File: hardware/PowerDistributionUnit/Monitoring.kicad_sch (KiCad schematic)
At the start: 19 parts, among them U32 ADS7953SBDBT, U33 MCP23S17-E/SS, U34 REF4132, U35 TLV9301xDBV

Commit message: added datasheets and footprints to PowerDistributionUnitLib symbol library
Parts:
- U32: footprint (none) -> Package_SO:TSSOP-38_4.4x9.7mm_P0.5mm
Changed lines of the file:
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@@
 			)
 		)
-		(property "Datasheet" ""
+		(property "Datasheet" "${KIPRJMOD}/lib/docs/ref4132.pdf"
 			(at 73.66 35.56 0)
 			(effects
@@
 			)
 		)
-		(property "Footprint" ""
+		(property "Footprint" "Package_SO:TSSOP-38_4.4x9.7mm_P0.5mm"
 			(at 111.76 80.01 0)
 			(effects
@@
 			)
 		)
-		(property "Datasheet" "https://www.ti.com/lit/ds/symlink/ads7953.pdf?ts=1728140483665&ref_url=https%253A%252F%252Fwww.ti.com%252Fproduct%252FADS7953%252Fpart-details%252FADS7953SBDBT"
+		(property "Datasheet" "${KIPRJMOD}/lib/docs/ads7953.pdf"
 			(at 111.76 80.01 0)
 			(effects
@@
 			)
 		)
-		(property "Datasheet" ""
+		(property "Datasheet" "${KIPRJMOD}/lib/docs/MCP23017-Data-Sheet-DS20001952-1.pdf"
 			(at 211.582 61.214 0)
 			(effects

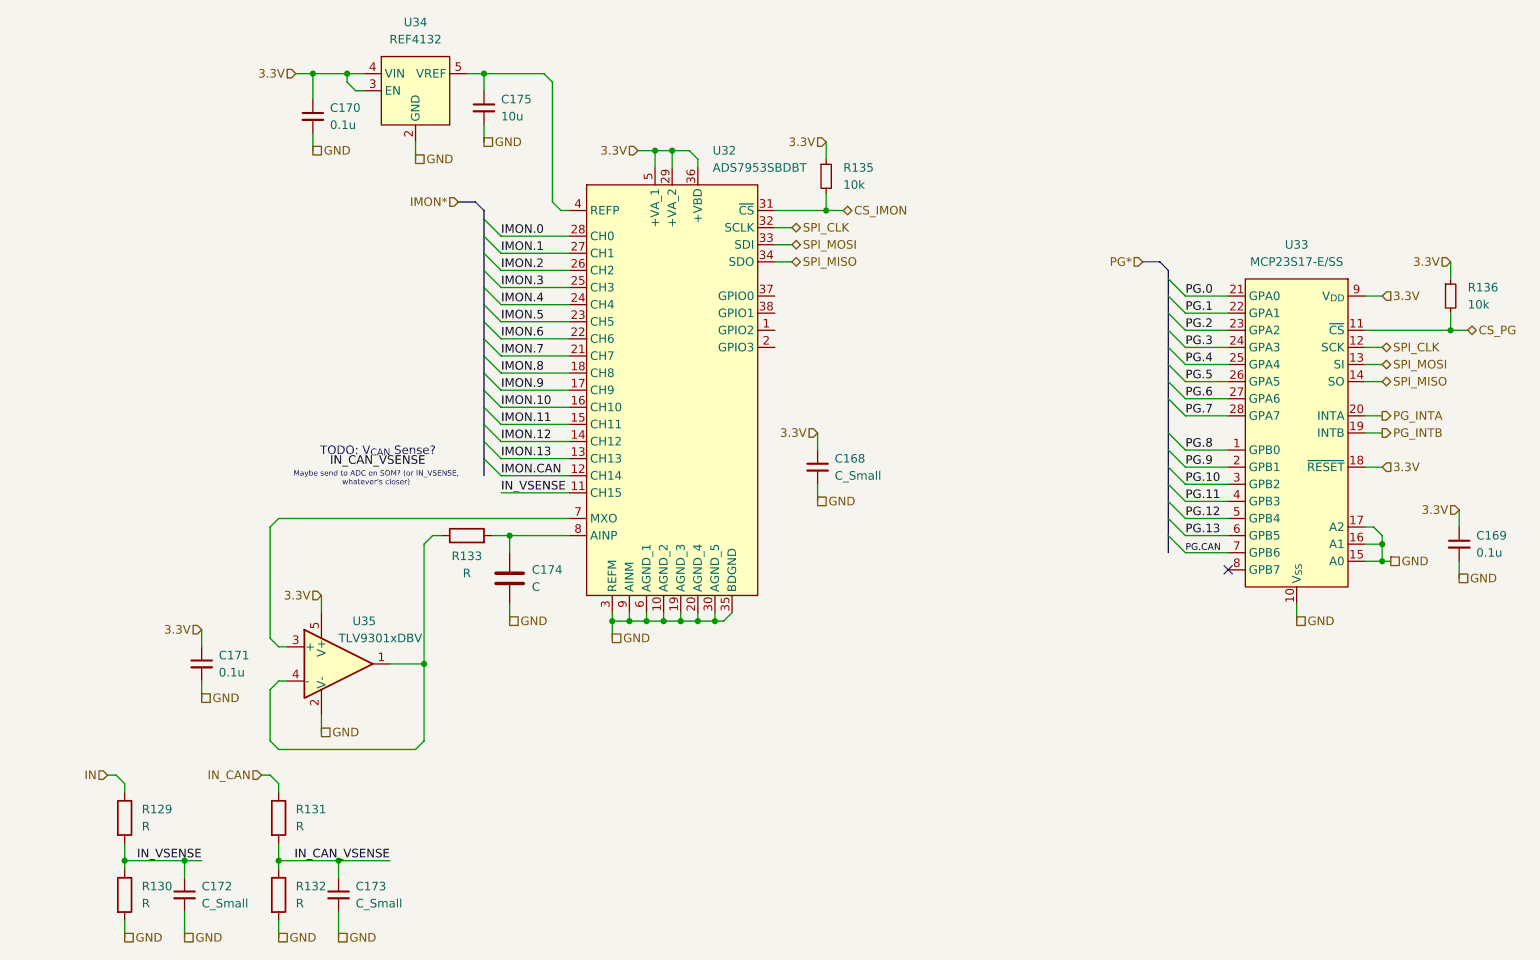
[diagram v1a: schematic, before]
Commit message: Continued revising eFuse isolation. Also fixed pulls on ADCMUX
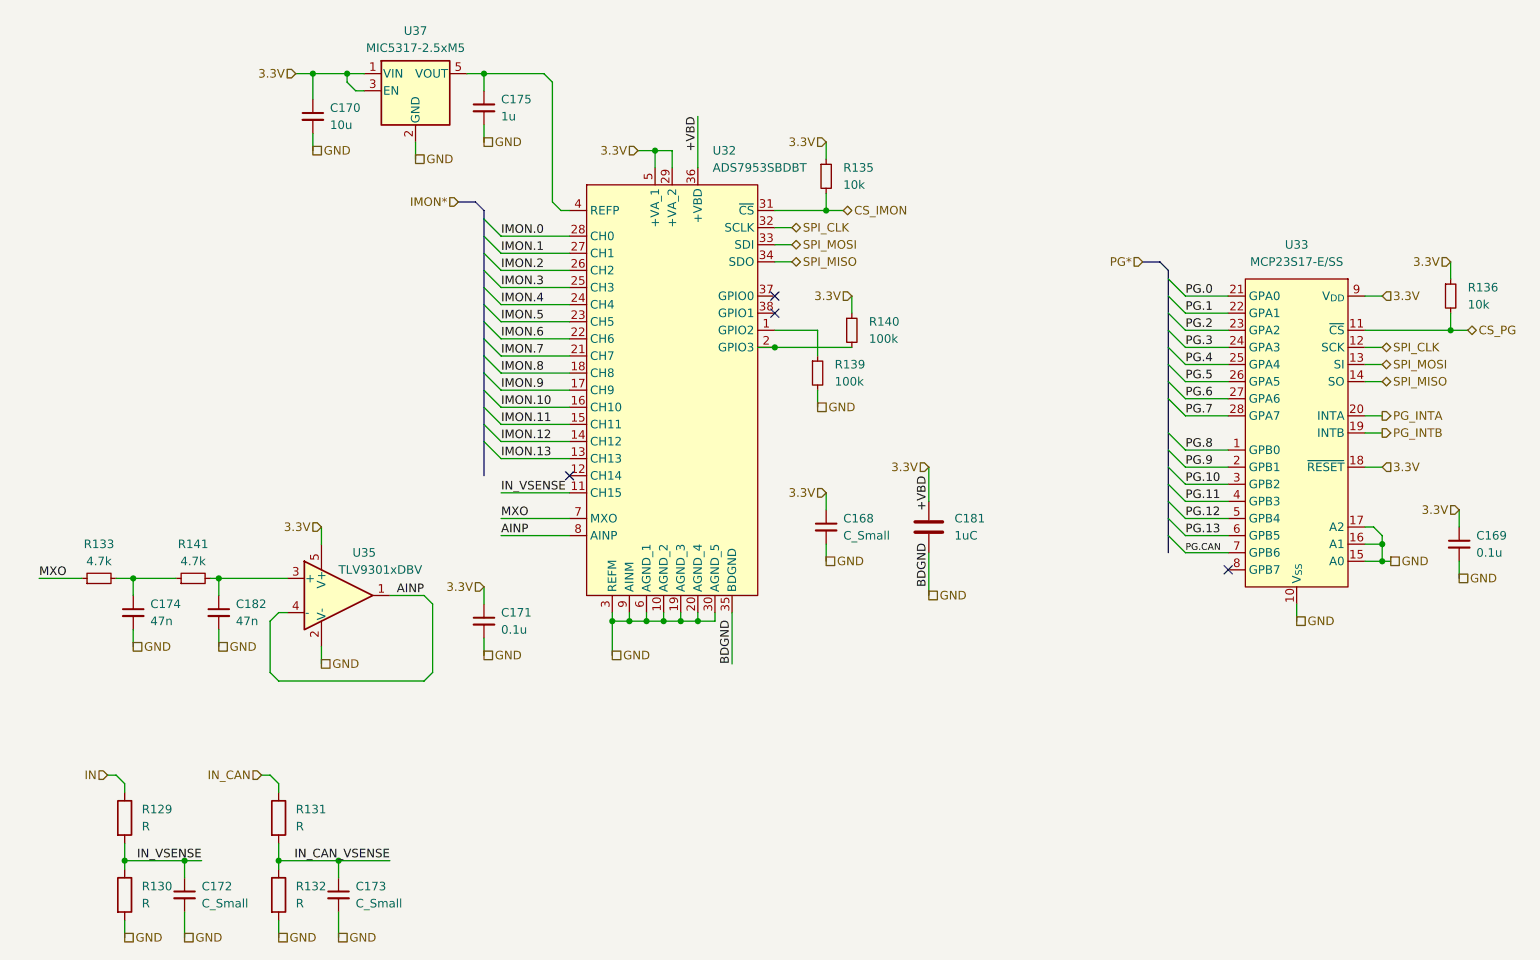
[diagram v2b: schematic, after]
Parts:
- removed C174: C, symbol Device:C
- removed R133: R, symbol Device:R
- removed U34: REF4132, Package_TO_SOT_SMD:SOT-23-5, symbol PowerDistributionUnitLib:REF4132
- added C174, C182: 47n, symbol Device:C_Small
- added C181: 1uC, symbol Device:C
- added R133, R141: 4.7k, symbol Device:R_Small
- added R139, R140: 100k, symbol Device:R_Small
- added U37: MIC5317-2.5xM5, Package_TO_SOT_SMD:SOT-23-5, symbol Regulator_Linear:MIC5317-2.5xM5
- C170: value 0.1u -> 10u
- C175: value 10u -> 1u
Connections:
- net 3.3V: now also C181.1, R140.1, U37.1 (VIN), U37.3 (EN)
- net GND: now also C174.2, C181.2, C182.2, R139.2, U37.2 (GND)
- net at C175.1, U32.4 (REFP): now also U37.5 (VOUT)
- net AINP: now reaches U35.1, U35.4 (-)
- net AINP: now also U32.8 (AINP)
- net at U32.1 (GPIO2): now also R139.1
- net at U32.2 (GPIO3): now also R140.2
- net at U35.3 (+): now also C182.1, R141.2; no longer U32.7 (MXO)
- net IMON.CAN: no longer names the net of U32.12 (CH14)
- new net: C174.1, R133.2, R141.1
- new net MXO: R133.1, U32.7 (MXO)
- no-connect marks 1 -> 4
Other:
- note removed: "Maybe send to ADC on SOM? (or IN_VSENSE, whatever's closer)"
- note removed: "TODO: V_{CAN} Sense?"
- moved on the sheet: C168, C171, U35

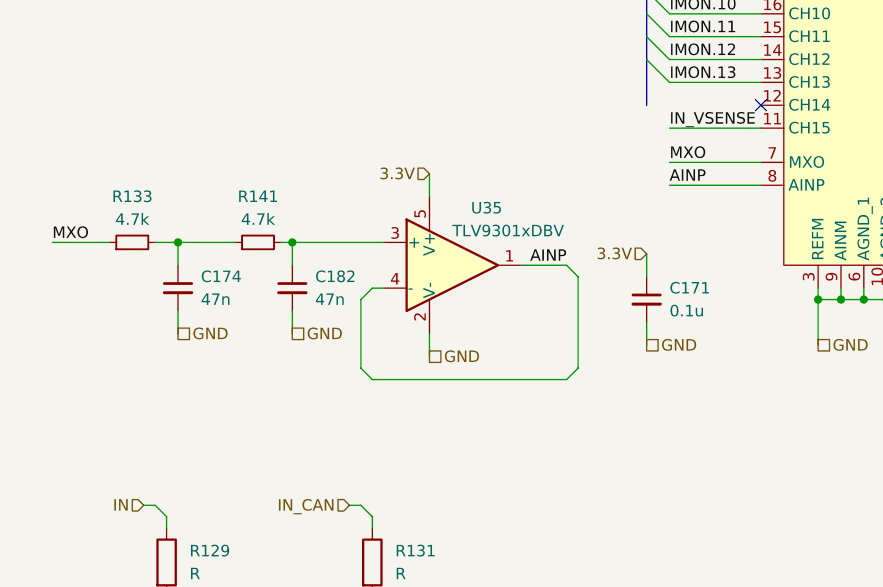
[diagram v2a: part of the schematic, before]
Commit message: Added footprints, added pull-up resistors, finished wiring up SOM
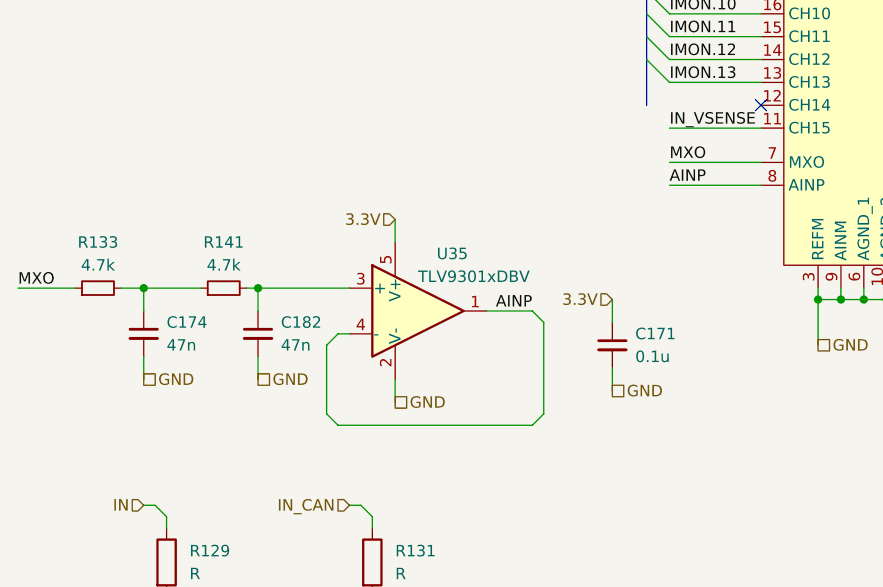
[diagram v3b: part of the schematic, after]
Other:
- moved on the sheet: C171, C174, C182, R133, R141, U35
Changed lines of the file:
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@@
 	(paper "A4")
 	(junction
-		(at 44.45 106.68)
+		(at 40.64 111.76)
 		(diameter 0)
 		(color 0 0 0 0)
@@
 	)
 	(junction
-		(at 31.75 106.68)
+		(at 27.94 111.76)
 		(diameter 0)
 		(color 0 0 0 0)
@@
 	(wire
 		(pts
-			(xy 74.93 109.22) (xy 76.2 110.49)
+			(xy 71.12 114.3) (xy 72.39 115.57)
 		)
 		(stroke
@@
 	(wire
 		(pts
-			(xy 29.21 106.68) (xy 31.75 106.68)
+			(xy 25.4 111.76) (xy 27.94 111.76)
 		)
 		(stroke
@@
 	(wire
 		(pts
-			(xy 59.69 99.06) (xy 59.69 101.6)
+			(xy 55.88 104.14) (xy 55.88 106.68)
 		)
 		(stroke
@@
 	(wire
 		(pts
-			(xy 69.85 109.22) (xy 74.93 109.22)
+			(xy 66.04 114.3) (xy 71.12 114.3)
 		)
 		(stroke
@@
 	(wire
 		(pts
-			(xy 17.78 106.68) (xy 24.13 106.68)
+			(xy 13.97 111.76) (xy 20.32 111.76)
 		)
 		(stroke
@@
 	(wire
 		(pts
-			(xy 74.93 121.92) (xy 76.2 120.65)
+			(xy 71.12 127) (xy 72.39 125.73)
 		)
 		(stroke
@@
 	(wire
 		(pts
-			(xy 83.82 107.95) (xy 83.82 110.49)
+			(xy 80.01 113.03) (xy 80.01 115.57)
 		)
 		(stroke
@@
 	(wire
 		(pts
-			(xy 83.82 115.57) (xy 83.82 118.11)
+			(xy 80.01 120.65) (xy 80.01 123.19)
 		)
 		(stroke
@@
 	(wire
 		(pts
-			(xy 59.69 119.38) (xy 59.69 116.84)
+			(xy 55.88 124.46) (xy 55.88 121.92)
 		)
 		(stroke
@@
 	(wire
 		(pts
-			(xy 52.07 120.65) (xy 53.34 121.92)
+			(xy 48.26 125.73) (xy 49.53 127)
 		)
 		(stroke
@@
 	(wire
 		(pts
-			(xy 31.75 106.68) (xy 31.75 109.22)
+			(xy 27.94 111.76) (xy 27.94 114.3)
 		)
 		(stroke
@@
 	(wire
 		(pts
-			(xy 43.18 106.68) (xy 44.45 106.68)
+			(xy 39.37 111.76) (xy 40.64 111.76)
 		)
 		(stroke
@@
 	(wire
 		(pts
-			(xy 44.45 106.68) (xy 44.45 109.22)
+			(xy 40.64 111.76) (xy 40.64 114.3)
 		)
 		(stroke
@@
 	(wire
 		(pts
-			(xy 53.34 111.76) (xy 54.61 111.76)
+			(xy 49.53 116.84) (xy 50.8 116.84)
 		)
 		(stroke
@@
 	(wire
 		(pts
-			(xy 31.75 106.68) (xy 38.1 106.68)
+			(xy 27.94 111.76) (xy 34.29 111.76)
 		)
 		(stroke
@@
 	(wire
 		(pts
-			(xy 76.2 110.49) (xy 76.2 120.65)
+			(xy 72.39 115.57) (xy 72.39 125.73)
 		)
 		(stroke
@@
 	(wire
 		(pts
-			(xy 44.45 106.68) (xy 54.61 106.68)
+			(xy 40.64 111.76) (xy 50.8 111.76)
 		)
 		(stroke
@@
 	(wire
 		(pts
-			(xy 53.34 111.76) (xy 52.07 113.03)
+			(xy 49.53 116.84) (xy 48.26 118.11)
 		)
 		(stroke
@@
 	(wire
 		(pts
-			(xy 44.45 116.84) (xy 44.45 114.3)
+			(xy 40.64 121.92) (xy 40.64 119.38)
 		)
 		(stroke
@@
 	(wire
 		(pts
-			(xy 53.34 121.92) (xy 74.93 121.92)
+			(xy 49.53 127) (xy 71.12 127)
 		)
 		(stroke
@@
 	(wire
 		(pts
-			(xy 52.07 113.03) (xy 52.07 120.65)
+			(xy 48.26 118.11) (xy 48.26 125.73)
 		)
 		(stroke
@@
 	(wire
 		(pts
-			(xy 31.75 116.84) (xy 31.75 114.3)
+			(xy 27.94 121.92) (xy 27.94 119.38)
 		)
 		(stroke
@@
 	)
 	(label "MXO"
-		(at 17.78 106.68 0)
+		(at 13.97 111.76 0)
 		(fields_autoplaced yes)
 		(effects
@@
 	)
 	(label "AINP"
-		(at 74.93 109.22 180)
+		(at 71.12 114.3 180)
 		(fields_autoplaced yes)
 		(effects
@@
 	(hierarchical_label "GND"
 		(shape passive)
-		(at 31.75 116.84 0)
+		(at 27.94 121.92 0)
 		(fields_autoplaced yes)
 		(effects
@@
 	(hierarchical_label "GND"
 		(shape passive)
-		(at 83.82 118.11 0)
+		(at 80.01 123.19 0)
 		(fields_autoplaced yes)
 		(effects
@@
 	(hierarchical_label "3.3V"
 		(shape input)
-		(at 83.82 107.95 180)
+		(at 80.01 113.03 180)
 		(fields_autoplaced yes)
 		(effects
@@
 	(hierarchical_label "GND"
 		(shape passive)
-		(at 59.69 119.38 0)
+		(at 55.88 124.46 0)
 		(fields_autoplaced yes)
 		(effects
@@
 	(hierarchical_label "3.3V"
 		(shape input)
-		(at 59.69 99.06 180)
+		(at 55.88 104.14 180)
 		(fields_autoplaced yes)
 		(effects
@@
 	(hierarchical_label "GND"
 		(shape passive)
-		(at 44.45 116.84 0)
+		(at 40.64 121.92 0)
 		(fields_autoplaced yes)
 		(effects
@@
 	(symbol
 		(lib_id "Device:C_Small")
-		(at 44.45 111.76 0)
+		(at 40.64 116.84 0)
 		(unit 1)
 		(exclude_from_sim no)
@@
 		(fields_autoplaced yes)
 		(property "Reference" "C182"
-			(at 46.99 110.4962 0)
+			(at 43.18 115.5762 0)
 			(effects
 				(font
@@
 		)
 		(property "Value" "47n"
-			(at 46.99 113.0362 0)
+			(at 43.18 118.1162 0)
 			(effects
 				(font
@@
 		)
 		(property "Footprint" ""
-			(at 44.45 111.76 0)
+			(at 40.64 116.84 0)
 			(effects
 				(font
@@
 		)
 		(property "Datasheet" "~"
-			(at 44.45 111.76 0)
+			(at 40.64 116.84 0)
 			(effects
 				(font
@@
 		)
 		(property "Description" "Unpolarized capacitor, small symbol"
-			(at 44.45 111.76 0)
+			(at 40.64 116.84 0)
 			(effects
 				(font
@@
 	(symbol
 		(lib_id "Device:R_Small")
-		(at 40.64 106.68 90)
+		(at 36.83 111.76 90)
 		(unit 1)
 		(exclude_from_sim no)
@@
 		(fields_autoplaced yes)
 		(property "Reference" "R141"
-			(at 40.64 101.6 90)
+			(at 36.83 106.68 90)
 			(effects
 				(font
@@
 		)
 		(property "Value" "4.7k"
-			(at 40.64 104.14 90)
+			(at 36.83 109.22 90)
 			(effects
 				(font
@@
 		)
 		(property "Footprint" ""
-			(at 40.64 106.68 0)
+			(at 36.83 111.76 0)
 			(effects
 				(font
@@
 		)
 		(property "Datasheet" "~"
-			(at 40.64 106.68 0)
+			(at 36.83 111.76 0)
 			(effects
 				(font
@@
 		)
 		(property "Description" "Resistor, small symbol"
-			(at 40.64 106.68 0)
+			(at 36.83 111.76 0)
 			(effects
 				(font
@@
 	(symbol
 		(lib_id "Device:C_Small")
-		(at 31.75 111.76 0)
+		(at 27.94 116.84 0)
 		(unit 1)
 		(exclude_from_sim no)
@@
 		(fields_autoplaced yes)
 		(property "Reference" "C174"
-			(at 34.29 110.4962 0)
+			(at 30.48 115.5762 0)
 			(effects
 				(font
@@
 		)
 		(property "Value" "47n"
-			(at 34.29 113.0362 0)
+			(at 30.48 118.1162 0)
 			(effects
 				(font
@@
 		)
 		(property "Footprint" ""
-			(at 31.75 111.76 0)
+			(at 27.94 116.84 0)
 			(effects
 				(font
@@
 		)
 		(property "Datasheet" "~"
-			(at 31.75 111.76 0)
+			(at 27.94 116.84 0)
 			(effects
 				(font
@@
 		)
 		(property "Description" "Unpolarized capacitor, small symbol"
-			(at 31.75 111.76 0)
+			(at 27.94 116.84 0)
 			(effects
 				(font
@@
 	(symbol
 		(lib_id "Device:R_Small")
-		(at 26.67 106.68 90)
+		(at 22.86 111.76 90)
 		(unit 1)
 		(exclude_from_sim no)
@@
 		(fields_autoplaced yes)
 		(property "Reference" "R133"
-			(at 26.67 101.6 90)
+			(at 22.86 106.68 90)
 			(effects
 				(font
@@
 		)
 		(property "Value" "4.7k"
-			(at 26.67 104.14 90)
+			(at 22.86 109.22 90)
 			(effects
 				(font
@@
 		)
 		(property "Footprint" ""
-			(at 26.67 106.68 0)
+			(at 22.86 111.76 0)
 			(effects
 				(font
@@
 		)
 		(property "Datasheet" "~"
-			(at 26.67 106.68 0)
+			(at 22.86 111.76 0)
 			(effects
 				(font
@@
 		)
 		(property "Description" "Resistor, small symbol"
-			(at 26.67 106.68 0)
+			(at 22.86 111.76 0)
 			(effects
 				(font
@@
 	(symbol
 		(lib_id "Device:C_Small")
-		(at 83.82 113.03 0)
+		(at 80.01 118.11 0)
 		(unit 1)
 		(exclude_from_sim no)
@@
 		(fields_autoplaced yes)
 		(property "Reference" "C171"
-			(at 86.36 111.7662 0)
+			(at 82.55 116.8462 0)
 			(effects
 				(font
@@
 		)
 		(property "Value" "0.1u"
-			(at 86.36 114.3062 0)
+			(at 82.55 119.3862 0)
 			(effects
 				(font
@@
 		)
 		(property "Footprint" ""
-			(at 83.82 113.03 0)
+			(at 80.01 118.11 0)
 			(effects
 				(font
@@
 		)
 		(property "Datasheet" "~"
-			(at 83.82 113.03 0)
+			(at 80.01 118.11 0)
 			(effects
 				(font
@@
 		)
 		(property "Description" "Unpolarized capacitor, small symbol"
-			(at 83.82 113.03 0)
+			(at 80.01 118.11 0)
 			(effects
 				(font
@@
 	(symbol
 		(lib_id "Amplifier_Operational:TLV9301xDBV")
-		(at 62.23 109.22 0)
+		(at 58.42 114.3 0)
 		(unit 1)
 		(exclude_from_sim no)
@@
 		(dnp no)
 		(property "Reference" "U35"
-			(at 66.04 102.87 0)
+			(at 62.23 107.95 0)
 			(effects
 				(font
@@
 		)
 		(property "Value" "TLV9301xDBV"
-			(at 62.23 105.41 0)
+			(at 58.42 110.49 0)
 			(effects
 				(font
@@
 		)
 		(property "Footprint" "Package_TO_SOT_SMD:SOT-23-5"
-			(at 59.69 114.3 0)
+			(at 55.88 119.38 0)
 			(effects
 				(font
@@
 		)
 		(property "Datasheet" "https://www.ti.com/lit/ds/symlink/tlv9301.pdf"
-			(at 62.23 104.14 0)
+			(at 58.42 109.22 0)
 			(effects
 				(font
@@
 		)
 		(property "Description" "40-V, 1-MHz, RRO Operational Amplifiers for Cost-Sensitive Systems, SOT-23-5"
-			(at 62.23 109.22 0)
+			(at 58.42 114.3 0)
 			(effects
 				(font
